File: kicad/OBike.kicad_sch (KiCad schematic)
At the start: 74 parts, among them J1 F34G-1A7Q1-E8C40, J2 Micro_SD_Card_Det1, J3 Conn_01x02, J4 Conn_01x04, J5 U.FL-R-SMT-1_10_, J6 Conn_01x02, J7 Conn_01x05, J8 Conn_01x02, Q1 SS8050, Q2 SS8050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

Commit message: updated part numbers
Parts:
- C2: MANUFACTURER (none) -> 1276-1066-1-ND
- Q1, Q2: Digikiey PN (none) -> MMSS8550-H-TPMSCT-ND
- R15, R38: Digikiey PN RMCF0805JT10K0CT-ND -> RMCF0603JT1K00CT-ND
- R18, R37: Digikiey PN RMCF0805JT10K0CT-ND -> RMCF0603JT10K0CT-ND
- R23, R24: Digikiey PN (none) -> RMCF0805JT10K0CT-ND
- R25: Digikiey PN (none) -> RMCF0603JT10K0CT-ND
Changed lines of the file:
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@@
 			)
 		)
-		(property "Digikiey PN" "RMCF0805JT10K0CT-ND"
+		(property "Digikiey PN" "RMCF0603JT1K00CT-ND"
 			(at 326.39 118.11 90)
 			(effects
@@
 			)
 		)
-		(property "MANUFACTURER" ""
+		(property "MANUFACTURER" "1276-1066-1-ND"
 			(at 60.96 30.48 0)
 			(effects
@@
 			)
 		)
+		(property "Digikiey PN" "MMSS8550-H-TPMSCT-ND"
+			(at 340.36 118.11 0)
+			(effects
+				(font
+					(size 1.27 1.27)
+				)
+				(hide yes)
+			)
+		)
 		(pin "3"
 		)
@@
 			)
 		)
-		(property "Digikiey PN" "RMCF0805JT10K0CT-ND"
+		(property "Digikiey PN" "RMCF0603JT1K00CT-ND"
 			(at 379.73 228.6 90)
 			(effects
@@
 			)
 		)
-		(property "Field6" ""
+		(property "Digikiey PN" "RMCF0805JT10K0CT-ND"
 			(at 29.21 214.63 90)
 			(effects
@@
 			)
 		)
-		(property "Field6" ""
+		(property "Digikiey PN" "RMCF0805JT10K0CT-ND"
 			(at 31.75 214.63 90)
 			(effects
@@
 			)
 		)
+		(property "Digikiey PN" "MMSS8550-H-TPMSCT-ND"
+			(at 393.7 228.6 0)
+			(effects
+				(font
+					(size 1.27 1.27)
+				)
+				(hide yes)
+			)
+		)
 		(pin "3"
 		)
@@
 			)
 		)
-		(property "Field6" ""
+		(property "Digikiey PN" "RMCF0603JT10K0CT-ND"
 			(at 26.67 214.63 90)
 			(effects
@@
 			)
 		)
-		(property "Digikiey PN" "RMCF0805JT10K0CT-ND"
+		(property "Digikiey PN" "RMCF0603JT10K0CT-ND"
 			(at 387.35 233.68 90)
 			(effects
@@
 			)
 		)
-		(property "Digikiey PN" "RMCF0805JT10K0CT-ND"
+		(property "Digikiey PN" "RMCF0603JT10K0CT-ND"
 			(at 334.01 124.46 90)
 			(effects

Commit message: fixed typo in part number fields
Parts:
- C1, C11, C13, C3: Digikey PN (none) -> 1276-2442-1-ND; Digikiey PN 1276-2442-1-ND -> (none)
- C10, C19: Digikey PN (none) -> 1276-1038-1-ND; Digikiey PN 1276-1038-1-ND -> (none)
- C12, C14, C4, C5, C6, C7, C8, C9: Digikey PN (none) -> 1276-1066-1-ND; Digikiey PN 1276-1066-1-ND -> (none)
- C16, C21: Digikey PN (none) -> 399-C0603C330K3RACTUCT-ND; Digikiey PN 399-C0603C330K3RACTUCT-ND -> (none)
- C17, C20: Digikey PN (none) -> 399-C0603C104K3RACTUCT-ND; Digikiey PN 399-C0603C104K3RACTUCT-ND -> (none)
- C18: Digikey PN (none) -> 1276-1044-1-ND; Digikiey PN 1276-1044-1-ND -> (none)
- D1, D2, D3, D4, D5: Digikey PN (none) -> 1655-1N4148WCT-ND; Digikiey PN 1655-1N4148WCT-ND -> (none)
- D6, D7: Digikey PN (none) -> 1727-2742-1-ND; Digikiey PN 1727-2742-1-ND -> (none)
- J1: Digikey PN (none) -> 609-F34G-1A7Q1-E8C40CT-ND; Digikiey PN 609-F34G-1A7Q1-E8C40CT-ND -> (none)
- J2: Digikey PN (none) -> 2223-MSD-4-ACT-ND; Digikiey PN 2223-MSD-4-ACT-ND -> (none)
- J3: Digikey PN (none) -> 455-1719-ND; Digikiey PN 455-1719-ND -> (none)
- J4, J6, J7, R13, R14, U5: now left out of the parts list
- J5: Digikey PN (none) -> H11891CT-ND; Digikiey PN H11891CT-ND -> (none)
- LS1: Digikey PN (none) -> 458-ASI09N40MTRQCT-ND
- Q1, Q2: Digikey PN (none) -> MMSS8550-H-TPMSCT-ND; Digikiey PN MMSS8550-H-TPMSCT-ND -> (none)
- R1, R10, R2, R22, R23, R24, R3, R36, R4, R5, R6, R7, R8, R9: Digikey PN (none) -> RMCF0805JT10K0CT-ND; Digikiey PN RMCF0805JT10K0CT-ND -> (none)
- R11, R16, R17: Digikey PN (none) -> RMCF0603FT100KCT-ND; Digikiey PN RMCF0603FT100KCT-ND -> (none)
- R12: Digikey PN (none) -> RMCF0603FT2R20CT-ND; Digikiey PN RMCF0603FT2R20CT-ND -> (none)
- R15, R38: Digikey PN (none) -> RMCF0603JT1K00CT-ND; Digikiey PN RMCF0603JT1K00CT-ND -> (none)
- R18, R25, R37: Digikey PN (none) -> RMCF0603JT10K0CT-ND; Digikiey PN RMCF0603JT10K0CT-ND -> (none)
- SW1: Digikey PN (none) -> 450-2425755-1CT-ND; Digikiey PN 450-2425755-1CT-ND -> (none)
- U1: Digikey PN (none) -> DPS368XTSA1CT-ND; Digikiey PN DPS368XTSA1CT-ND -> (none)
- U10, U6, U8: Digikey PN (none) -> MAX40200AUK+TCT-ND; Digikiey PN MAX40200AUK+TCT-ND -> (none)
- U2: Digikey PN (none) -> DS3231MZ+-ND; Digikiey PN DS3231MZ+-ND -> (none)
- U3: Digikey PN (none) -> MCP23017T-E/SOCT-ND; Digikiey PN MCP23017T-E/SOCT-ND -> (none)
- U4: Digikey PN (none) -> 74HC14DCT-ND; Digikiey PN 74HC14DCT-ND -> (none)
- U7: Digikey PN (none) -> 2958-LC76GPAMDCT-ND; Digikiey PN 2958-LC76GPAMDCT-ND -> (none)
- U9: Digikey PN (none) -> 256-W25N01GVZEIGTRCT-ND; Digikiey PN 256-W25N01GVZEIGTRCT-ND -> (none)

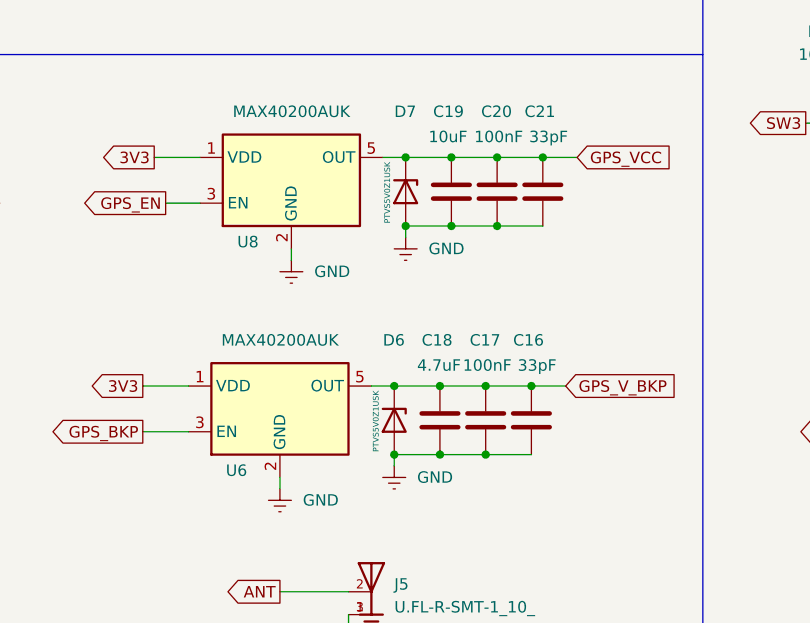
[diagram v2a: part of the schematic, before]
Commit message: zenners went EOL updated to new device
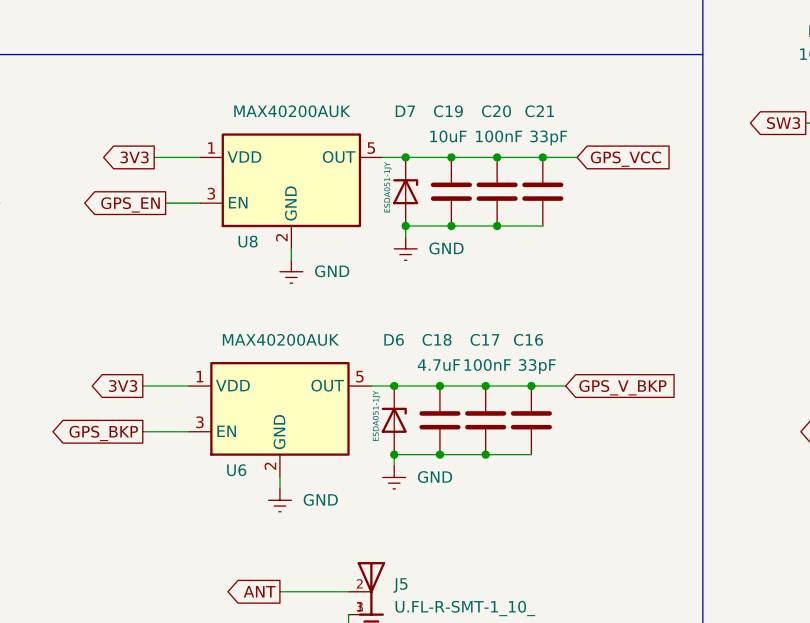
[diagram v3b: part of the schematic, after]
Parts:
- D6, D7: value PTVS5V0Z1USK -> ESDA051-1JY; footprint Diode_SMD:Nexperia_DSN1608-2_1.6x0.8mm -> Diode_SMD:D_SOD-323; Digikey PN 1727-2742-1-ND -> 497-ESDA051-1JYCT-ND
- J8: now left out of the parts list
- R25: Digikey PN RMCF0603JT10K0CT-ND -> RMCF0805JT10K0CT-ND
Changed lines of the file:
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@@
 	)
 	(junction
+		(at 144.78 107.95)
+		(diameter 0)
+		(color 0 0 0 0)
+	)
+	(junction
 		(at 50.8 154.94)
 		(diameter 0)
@@
 	)
 	(junction
-		(at 144.78 115.57)
-		(diameter 0)
-		(color 0 0 0 0)
-	)
-	(junction
 		(at 378.46 110.49)
 		(diameter 0)
@@
 	)
 	(junction
-		(at 139.7 48.26)
+		(at 144.78 115.57)
 		(diameter 0)
 		(color 0 0 0 0)
 	)
 	(junction
-		(at 151.13 90.17)
+		(at 139.7 48.26)
 		(diameter 0)
 		(color 0 0 0 0)
 	)
 	(junction
-		(at 160.02 107.95)
+		(at 151.13 90.17)
 		(diameter 0)
 		(color 0 0 0 0)
 	)
 	(junction
-		(at 144.78 107.95)
+		(at 160.02 107.95)
 		(diameter 0)
 		(color 0 0 0 0)
@@
 	(wire
 		(pts
-			(xy 149.86 107.95) (xy 144.78 107.95)
+			(xy 142.24 107.95) (xy 144.78 107.95)
 		)
 		(stroke
@@
 	(wire
 		(pts
-			(xy 142.24 107.95) (xy 144.78 107.95)
-		)
-		(stroke
-			(width 0)
-			(type default)
-		)
-	)
-	(wire
-		(pts
 			(xy 377.19 85.09) (xy 382.27 85.09)
 		)
@@
 	(wire
 		(pts
+			(xy 144.78 107.95) (xy 149.86 107.95)
+		)
+		(stroke
+			(width 0)
+			(type default)
+		)
+	)
+	(wire
+		(pts
 			(xy 132.08 118.11) (xy 132.08 119.38)
 		)
@@
 			)
 		)
-		(property "Value" "PTVS5V0Z1USK"
+		(property "Value" "ESDA051-1JY"
 			(at 144.018 83.058 0)
 			(effects
@@
 			)
 		)
-		(property "Footprint" "Diode_SMD:Nexperia_DSN1608-2_1.6x0.8mm"
+		(property "Footprint" "Diode_SMD:D_SOD-323"
 			(at 141.605 86.36 0)
 			(effects
@@
 			)
 		)
-		(property "Datasheet" "https://assets.nexperia.com/documents/data-sheet/PTVS5V0Z1USK.pdf"
+		(property "Datasheet" "https://www.st.com/resource/en/datasheet/esda051-1jy.pdf"
 			(at 146.05 86.36 0)
 			(effects
@@
 			)
 		)
-		(property "Description" "5V, 1200W TVS unidirectional diode, DSN1608-2"
+		(property "Description" "TVS DIODE 5VWM 12.8VC SOD323"
 			(at 146.05 86.36 0)
 			(effects
@@
 			)
 		)
-		(property "Digikey PN" "1727-2742-1-ND"
-			(at 146.05 86.36 90)
-			(effects
-				(font
-					(size 1.27 1.27)
-				)
-				(hide yes)
-			)
-		)
-		(property "Digikiey PN" ""
+		(property "Digikey PN" "497-ESDA051-1JYCT-ND"
 			(at 146.05 86.36 90)
 			(effects
@@
 		(unit 1)
 		(exclude_from_sim no)
-		(in_bom yes)
+		(in_bom no)
 		(on_board yes)
 		(dnp no)
@@
 			)
 		)
-		(property "Digikiey PN" ""
-			(at 27.94 190.5 90)
+		(pin "1"
+		)
+		(pin "2"
+		)
+		(instances
+			(project "OBike"
+				(path "/b6c91502-91b9-44d0-9569-7774925b5f71"
+					(reference "R22")
+					(unit 1)
+				)
+			)
+		)
+	)
+	(symbol
+		(lib_id "Diode:PTVS5V0Z1USK")
+		(at 144.78 111.76 270)
+		(unit 1)
+		(exclude_from_sim no)
+		(in_bom yes)
+		(on_board yes)
+		(dnp no)
+		(property "Reference" "D6"
+			(at 143.51 102.87 90)
+			(effects
+				(font
+					(size 1.27 1.27)
+				)
+				(justify left)
+			)
+		)
+		(property "Value" "ESDA051-1JY"
+			(at 142.748 108.458 0)
+			(effects
+				(font
+					(size 0.635 0.635)
+				)
+				(justify left)
+			)
+		)
+		(property "Footprint" "Diode_SMD:D_SOD-323"
+			(at 140.335 111.76 0)
+			(effects
+				(font
+					(size 1.27 1.27)
+				)
+				(hide yes)
+			)
+		)
+		(property "Datasheet" "https://www.st.com/resource/en/datasheet/esda051-1jy.pdf"
+			(at 144.78 111.76 0)
+			(effects
+				(font
+					(size 1.27 1.27)
+				)
+				(hide yes)
+			)
+		)
+		(property "Description" "TVS DIODE 5VWM 12.8VC SOD323"
+			(at 144.78 111.76 0)
+			(effects
+				(font
+					(size 1.27 1.27)
+				)
+				(hide yes)
+			)
+		)
+		(property "Digikey PN" "497-ESDA051-1JYCT-ND"
+			(at 144.78 111.76 90)
 			(effects
 				(font
@@
 			(project "OBike"
 				(path "/b6c91502-91b9-44d0-9569-7774925b5f71"
-					(reference "R22")
+					(reference "D6")
 					(unit 1)
 				)
@@
 			)
 		)
-		(property "Digikiey PN" ""
-			(at 29.21 214.63 90)
-			(effects
-				(font
-					(size 1.27 1.27)
-				)
-				(hide yes)
-			)
-		)
 		(pin "1"
 		)
@@
 			)
 		)
-		(property "Digikiey PN" ""
-			(at 31.75 214.63 90)
-			(effects
-				(font
-					(size 1.27 1.27)
-				)
-				(hide yes)
-			)
-		)
 		(pin "1"
 		)
@@
 	)
 	(symbol
-		(lib_id "Diode:PTVS5V0Z1USK")
-		(at 144.78 111.76 270)
-		(unit 1)
-		(exclude_from_sim no)
-		(in_bom yes)
-		(on_board yes)
-		(dnp no)
-		(property "Reference" "D6"
-			(at 143.51 102.87 90)
-			(effects
-				(font
-					(size 1.27 1.27)
-				)
-				(justify left)
-			)
-		)
-		(property "Value" "PTVS5V0Z1USK"
-			(at 142.748 108.458 0)
-			(effects
-				(font
-					(size 0.635 0.635)
-				)
-				(justify left)
-			)
-		)
-		(property "Footprint" "Diode_SMD:Nexperia_DSN1608-2_1.6x0.8mm"
-			(at 140.335 111.76 0)
-			(effects
-				(font
-					(size 1.27 1.27)
-				)
-				(hide yes)
-			)
-		)
-		(property "Datasheet" "https://assets.nexperia.com/documents/data-sheet/PTVS5V0Z1USK.pdf"
-			(at 144.78 111.76 0)
-			(effects
-				(font
-					(size 1.27 1.27)
-				)
-				(hide yes)
-			)
-		)
-		(property "Description" "5V, 1200W TVS unidirectional diode, DSN1608-2"
-			(at 144.78 111.76 0)
-			(effects
-				(font
-					(size 1.27 1.27)
-				)
-				(hide yes)
-			)
-		)
-		(property "Digikey PN" "1727-2742-1-ND"
-			(at 144.78 111.76 90)
-			(effects
-				(font
-					(size 1.27 1.27)
-				)
-				(hide yes)
-			)
-		)
-		(property "Digikiey PN" ""
-			(at 144.78 111.76 90)
-			(effects
-				(font
-					(size 1.27 1.27)
-				)
-				(hide yes)
-			)
-		)
-		(pin "1"
-		)
-		(pin "2"
-		)
-		(instances
-			(project ""
-				(path "/b6c91502-91b9-44d0-9569-7774925b5f71"
-					(reference "D6")
-					(unit 1)
-				)
-			)
-		)
-	)
-	(symbol
 		(lib_id "Device:R")
 		(at 26.67 214.63 0)
@@
 			)
 		)
-		(property "Digikey PN" "RMCF0603JT10K0CT-ND"
-			(at 26.67 214.63 90)
-			(effects
-				(font
-					(size 1.27 1.27)
-				)
-				(hide yes)
-			)
-		)
-		(property "Digikiey PN" ""
+		(property "Digikey PN" "RMCF0805JT10K0CT-ND"
 			(at 26.67 214.63 90)
 			(effects
